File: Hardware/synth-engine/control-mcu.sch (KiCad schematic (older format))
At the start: 75 parts, among them J1 SWD_programming, J2 USB, J3 MIDI_IN, J4 MIDI_OUT, Q1 2N3904, U1 CY8C4246AZI-L445, U2 4N28, Y1 16MHz

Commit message: route 3.3VD voltage regulator and control MCU
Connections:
- net +5V: no longer C1.1, C3.1, C4.1, C5.1, C6.2, C7.1, C8.1, C9.2, J1.1 (Pin_1), R2.1, U1.11 (VDDA), U1.17 (VSSIO), U1.50 (VDDD), U1.56 (VDDA)
- net 3.3V: now also C1.1, C3.1, C4.1, C5.1, C6.2, C7.1, C8.1, C9.2, J1.1 (Pin_1), R2.1, U1.11 (VDDA), U1.17 (VSSIO), U1.50 (VDDD), U1.56 (VDDA)
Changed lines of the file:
@@
-	1    0    0    -1
-$EndComp
-$Comp
-L power:+5V #PWR012
-U 1 1 5DDBF5E4
-P 1400 1250
-F 0 "#PWR012" H 1400 1100 50  0001 C CNN
-F 1 "+5V" H 1415 1423 50  0000 C CNN
-F 2 "" H 1400 1250 50  0001 C CNN
-F 3 "" H 1400 1250 50  0001 C CNN
-	1    1400 1250
 	1    0    0    -1
 $EndComp
@@
 Wire Wire Line
 	1050 1800 1600 1800
-$Comp
-L power:+5V #PWR06
-U 1 1 5DDBF5FB
-P 950 2750
-F 0 "#PWR06" H 950 2600 50  0001 C CNN
-F 1 "+5V" H 965 2923 50  0000 C CNN
-F 2 "" H 950 2750 50  0001 C CNN
-F 3 "" H 950 2750 50  0001 C CNN
-	1    950  2750
-	1    0    0    -1
-$EndComp
 $Comp
 L power:GNDD #PWR07
@@
 Connection ~ 950  3000
 $Comp
-L power:+5V #PWR01
-U 1 1 5DDBF61B
-P 650 3200
-F 0 "#PWR01" H 650 3050 50  0001 C CNN
-F 1 "+5V" H 665 3373 50  0000 C CNN
-F 2 "" H 650 3200 50  0001 C CNN
-F 3 "" H 650 3200 50  0001 C CNN
-	1    650  3200
-	1    0    0    -1
-$EndComp
-$Comp
 L power:GNDD #PWR02
 U 1 1 5DDBF621
@@
 Connection ~ 650  3450
 $Comp
-L power:+5V #PWR04
-U 1 1 5DDBF63B
-P 850 3600
-F 0 "#PWR04" H 850 3450 50  0001 C CNN
-F 1 "+5V" H 950 3650 50  0000 C CNN
-F 2 "" H 850 3600 50  0001 C CNN
-F 3 "" H 850 3600 50  0001 C CNN
-	1    850  3600
-	1    0    0    -1
-$EndComp
-$Comp
 L power:GNDD #PWR05
 U 1 1 5DDBF641
@@
 Wire Wire Line
 	1600 3850 1600 3750
-$Comp
-L power:+5V #PWR09
-U 1 1 5DDBF65E
-P 1050 4250
-F 0 "#PWR09" H 1050 4100 50  0001 C CNN
-F 1 "+5V" H 1065 4423 50  0000 C CNN
-F 2 "" H 1050 4250 50  0001 C CNN
-F 3 "" H 1050 4250 50  0001 C CNN
-	1    1050 4250
-	1    0    0    1
-$EndComp
 $Comp
 L power:GNDD #PWR08
@@
 Wire Wire Line
 	1200 7250 950  7250
-$Comp
-L power:+5V #PWR010
-U 1 1 5DDBF6E8
-P 1050 7000
-F 0 "#PWR010" H 1050 6850 50  0001 C CNN
-F 1 "+5V" H 1150 7050 50  0000 C CNN
-F 2 "" H 1050 7000 50  0001 C CNN
-F 3 "" H 1050 7000 50  0001 C CNN
-	1    1050 7000
-	1    0    0    -1
-$EndComp
 Wire Wire Line
 	1050 7000 1050 7150
@@
 Wire Wire Line
 	1450 2350 1600 2350
+$Comp
+L SparkFun-Aesthetics:3.3V #SUPPLY?
+U 1 1 5DDD3D34
+P 1400 1250
+F 0 "#SUPPLY?" H 1400 1250 50  0001 L BNN
+F 1 "3.3V" H 1400 1424 50  0000 C CNN
+F 2 "" H 1400 1250 50  0001 C CNN
+F 3 "" H 1400 1250 50  0001 C CNN
+	1    1400 1250
+	1    0    0    -1
+$EndComp
+$Comp
+L SparkFun-Aesthetics:3.3V #SUPPLY?
+U 1 1 5DDD5545
+P 950 2750
+F 0 "#SUPPLY?" H 950 2750 50  0001 L BNN
+F 1 "3.3V" H 950 2924 50  0000 C CNN
+F 2 "" H 950 2750 50  0001 C CNN
+F 3 "" H 950 2750 50  0001 C CNN
+	1    950  2750
+	1    0    0    -1
+$EndComp
+$Comp
+L SparkFun-Aesthetics:3.3V #SUPPLY?
+U 1 1 5DDD6153
+P 650 3200
+F 0 "#SUPPLY?" H 650 3200 50  0001 L BNN
+F 1 "3.3V" H 650 3374 50  0000 C CNN
+F 2 "" H 650 3200 50  0001 C CNN
+F 3 "" H 650 3200 50  0001 C CNN
+	1    650  3200
+	1    0    0    -1
+$EndComp
+$Comp
+L SparkFun-Aesthetics:3.3V #SUPPLY?
+U 1 1 5DDD61F4
+P 850 3600
+F 0 "#SUPPLY?" H 850 3600 50  0001 L BNN
+F 1 "3.3V" H 1000 3650 50  0000 C CNN
+F 2 "" H 850 3600 50  0001 C CNN
+F 3 "" H 850 3600 50  0001 C CNN
+	1    850  3600
+	1    0    0    -1
+$EndComp
+$Comp
+L SparkFun-Aesthetics:3.3V #SUPPLY?
+U 1 1 5DDD6380
+P 1050 4250
+F 0 "#SUPPLY?" H 1050 4250 50  0001 L BNN
+F 1 "3.3V" H 1050 4424 50  0000 C CNN
+F 2 "" H 1050 4250 50  0001 C CNN
+F 3 "" H 1050 4250 50  0001 C CNN
+	1    1050 4250
+	-1   0    0    1
+$EndComp
+$Comp
+L SparkFun-Aesthetics:3.3V #SUPPLY?
+U 1 1 5DDD845B
+P 1050 7000
+F 0 "#SUPPLY?" H 1050 7000 50  0001 L BNN
+F 1 "3.3V" H 1050 7174 50  0000 C CNN
+F 2 "" H 1050 7000 50  0001 C CNN
+F 3 "" H 1050 7000 50  0001 C CNN
+	1    1050 7000
+	1    0    0    -1
+$EndComp
 $EndSCHEMATC

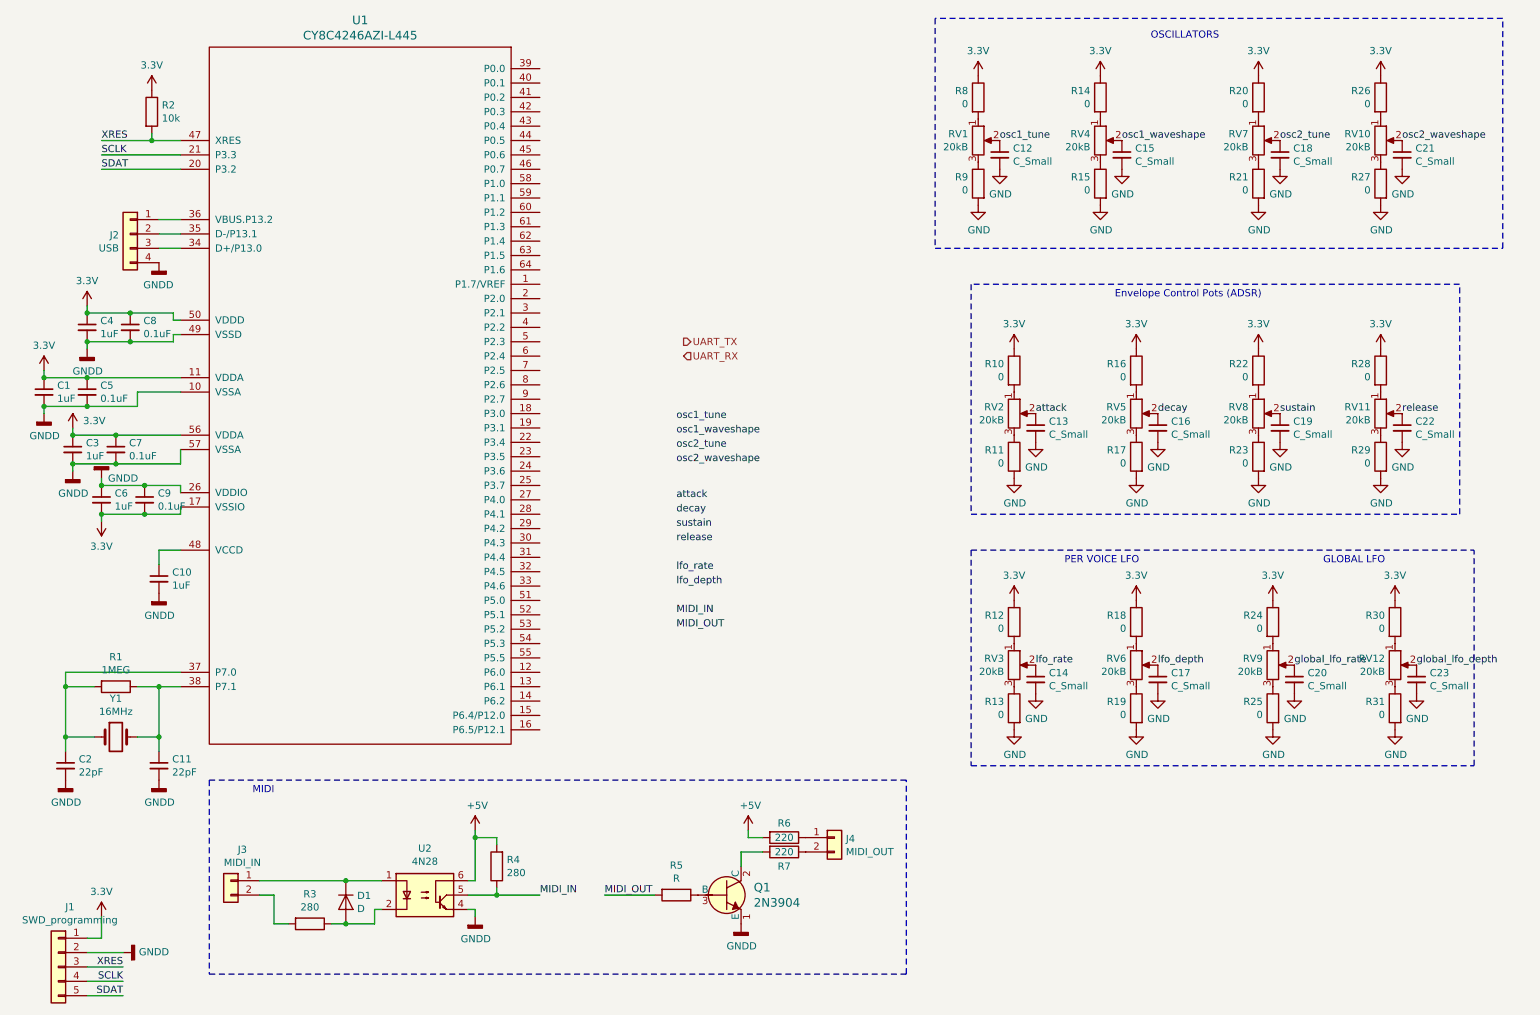
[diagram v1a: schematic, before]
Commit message: add separate PCB with potentiometers and switches and connector between control board and synth engine
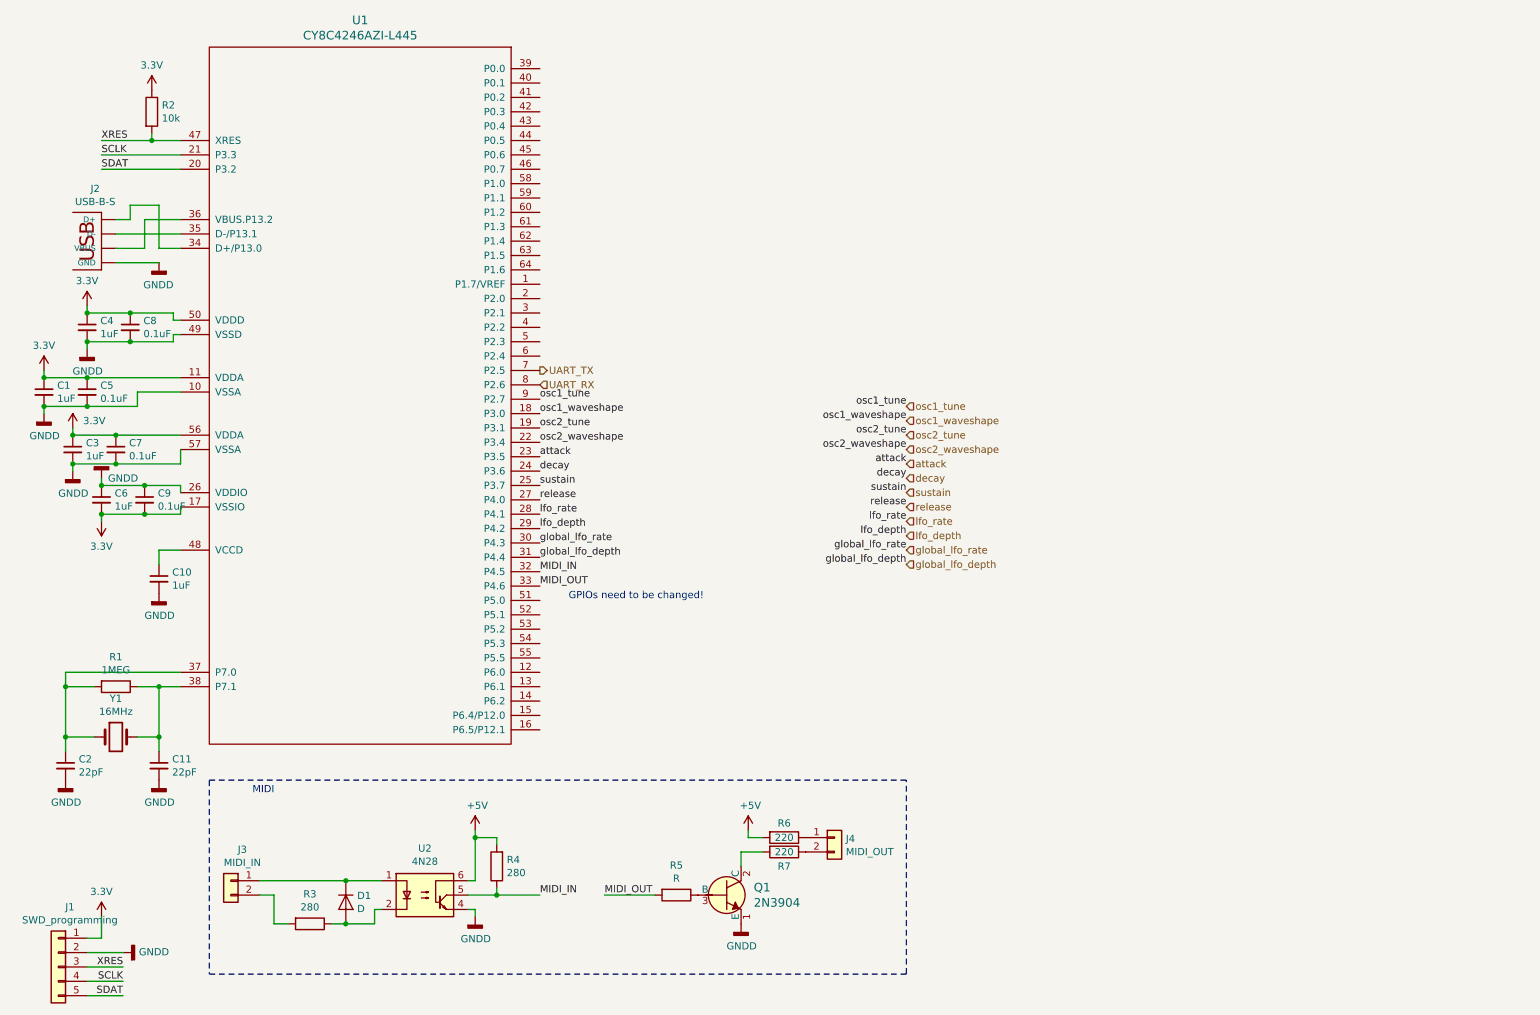
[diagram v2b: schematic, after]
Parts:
- removed C12, C13, C14, C15, C16, C17, C18, C19, C20, C21, C22, C23: C_Small, SparkFun-Passives:0805, symbol Device:C_Small
- removed J2: USB, SparkFun-Connectors:USB-B-PTH, symbol Connector_Generic:Conn_01x04
- removed R10, R11, R12, R13, R14, R15, R16, R17, R18, R19, R20, R21, R22, R23, R24, R25, R26, R27, R28, R29, R30, R31, R8, R9: 0, SparkFun-Passives:0805, symbol Device:R
- removed RV1, RV10, RV11, RV12, RV2, RV3, RV4, RV5, RV6, RV7, RV8, RV9: 20kB, Potentiometer_THT:Potentiometer_Alps_RK09K_Single_Vertical, symbol Device:R_POT
- added J2: USB-B-S, SparkFun-Connectors:USB-B-PTH, symbol SparkFun-Connectors:USB-B-S
- D1: footprint SparkFun-DiscreteSemi:SMB-DIODE -> SparkFun-Passives:1210
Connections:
- net GNDD: now also J2.GND
- net MIDI_IN: now also U1.32 (P4.5)
- net MIDI_OUT: now also U1.33 (P4.6)
- net UART_RX: now also U1.8 (P2.6)
- net UART_TX: now also U1.7 (P2.5)
- net attack: now also U1.23 (P3.5)
- net decay: now also U1.24 (P3.6)
- net global_lfo_depth: now also U1.31 (P4.4)
- net global_lfo_rate: now also U1.30 (P4.3)
- net lfo_depth: now also U1.29 (P4.2)
- net lfo_rate: now also U1.28 (P4.1)
- net osc1_tune: now also U1.9 (P2.7)
- net osc1_waveshape: now also U1.18 (P3.0)
- net osc2_tune: now also U1.19 (P3.1)
- net osc2_waveshape: now also U1.22 (P3.4)
- net release: now also U1.27 (P4.0)
- net sustain: now also U1.25 (P3.7)
- net at U1.34 (D+/P13.0): now also J2.D+
- net at U1.35 (D-/P13.1): now also J2.D-
- net at U1.36 (VBUS.P13.2): now also J2.VUSB (VBUS)
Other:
- note added: "GPIOs need to be changed!"
- note removed: "Envelope Control Pots (ADSR)"
- note removed: "GLOBAL LFO"
- note removed: "OSCILLATORS"
- note removed: "PER VOICE LFO"

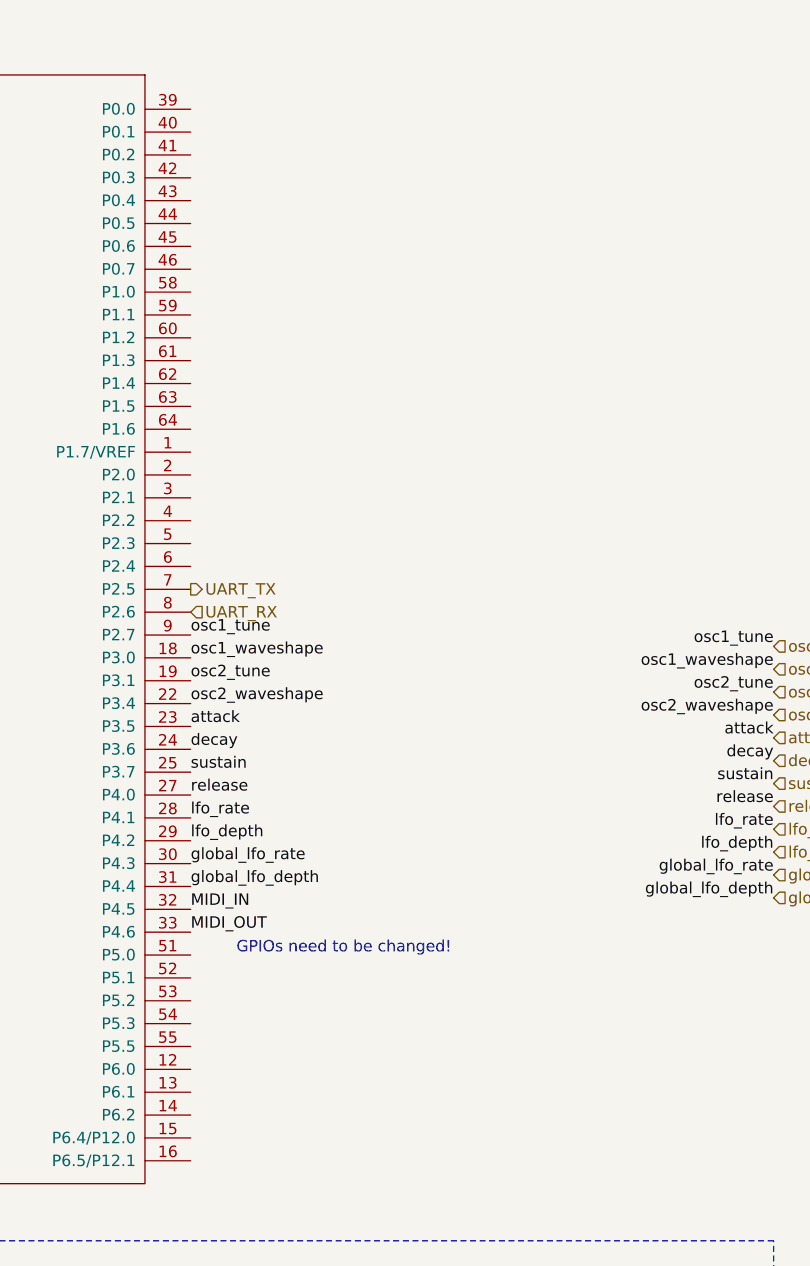
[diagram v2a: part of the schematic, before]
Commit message: initial routing complete. Still need to do ground plane pours. There are still some issues with incorrect footprints.
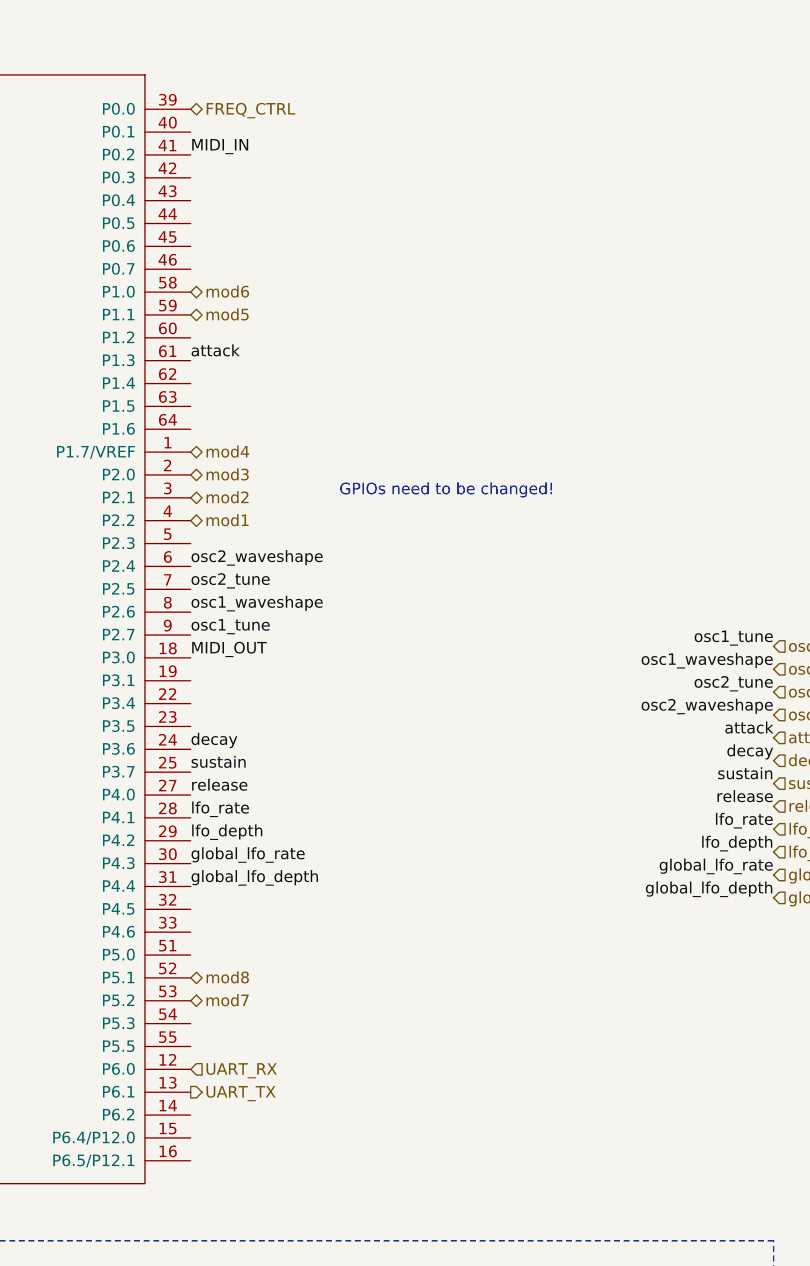
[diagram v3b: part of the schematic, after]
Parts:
- U2: footprint Package_DIP:DIP-6_W7.62mm -> SparkFun-AnalogIC:DIL-08
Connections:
- net MIDI_IN: now also U1.41 (P0.2); no longer U1.32 (P4.5)
- net MIDI_OUT: now also U1.18 (P3.0); no longer U1.33 (P4.6)
- net UART_RX: now also U1.12 (P6.0); no longer U1.8 (P2.6)
- net UART_TX: now also U1.13 (P6.1); no longer U1.7 (P2.5)
- net attack: now also U1.61 (P1.3); no longer U1.23 (P3.5)
- net osc1_waveshape: now also U1.8 (P2.6); no longer U1.18 (P3.0)
- net osc2_tune: now also U1.7 (P2.5); no longer U1.19 (P3.1)
- net osc2_waveshape: now also U1.6 (P2.4); no longer U1.22 (P3.4)
- net mod4: now reaches U1.1 (P1.7/VREF)
- net mod3: now reaches U1.2 (P2.0)
- net mod2: now reaches U1.3 (P2.1)
- net FREQ_CTRL: now reaches U1.39 (P0.0)
- net mod1: now reaches U1.4 (P2.2)
- net mod8: now reaches U1.52 (P5.1)
- net mod7: now reaches U1.53 (P5.2)
- net mod6: now reaches U1.58 (P1.0)
- net mod5: now reaches U1.59 (P1.1)
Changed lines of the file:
@@
 F 0 "U2" H 3300 7175 50  0000 C CNN
 F 1 "4N28" H 3300 7084 50  0000 C CNN
-F 2 "Package_DIP:DIP-6_W7.62mm" H 3100 6650 50  0001 L CIN
+F 2 "SparkFun-AnalogIC:DIL-08" H 3100 6650 50  0001 L CIN
 F 3 "https://www.vishay.com/docs/83725/4n25.pdf" H 3300 6850 50  0001 L CNN
 	1    3300 6850
@@
 Text Label 6650 4350 2    50   ~ 0
 lfo_depth
-Text Label 4100 4600 0    50   ~ 0
+Text Label 4100 1300 0    50   ~ 0
 MIDI_IN
-Text Label 4100 4700 0    50   ~ 0
+Text Label 4100 3500 0    50   ~ 0
 MIDI_OUT
 $Comp
@@
 Text Label 6650 3750 2    50   ~ 0
 osc2_waveshape
-Text HLabel 4100 3200 2    50   Output ~ 0
+Text HLabel 4100 5400 2    50   Output ~ 0
 UART_TX
-Text HLabel 4100 3300 2    50   Input ~ 0
+Text HLabel 4100 5300 2    50   Input ~ 0
 UART_RX
 Wire Wire Line
@@
 Text Label 6650 4550 2    50   ~ 0
 global_lfo_depth
-Text Label 4100 3800 0    50   ~ 0
+Text Label 4100 2200 0    50   ~ 0
 attack
 Text Label 4100 3900 0    50   ~ 0
@@
 Text Label 4100 3400 0    50   ~ 0
 osc1_tune
-Text Label 4100 3500 0    50   ~ 0
+Text Label 4100 3300 0    50   ~ 0
 osc1_waveshape
-Text Label 4100 3600 0    50   ~ 0
+Text Label 4100 3200 0    50   ~ 0
 osc2_tune
-Text Label 4100 3700 0    50   ~ 0
+Text Label 4100 3100 0    50   ~ 0
 osc2_waveshape
 Text Label 4100 4400 0    50   ~ 0
@@
 Text Label 4100 4500 0    50   ~ 0
 global_lfo_depth
-Text Notes 4300 4800 0    50   ~ 0
+Text Notes 4750 2800 0    50   ~ 0
 GPIOs need to be changed!
+Text HLabel 4100 1100 2    50   BiDi ~ 0
+FREQ_CTRL
+Text HLabel 4100 2900 2    50   BiDi ~ 0
+mod1
+Text HLabel 4100 2800 2    50   BiDi ~ 0
+mod2
+Text HLabel 4100 2700 2    50   BiDi ~ 0
+mod3
+Text HLabel 4100 2600 2    50   BiDi ~ 0
+mod4
+Text HLabel 4100 2000 2    50   BiDi ~ 0
+mod5
+Text HLabel 4100 1900 2    50   BiDi ~ 0
+mod6
+Text HLabel 4100 5000 2    50   BiDi ~ 0
+mod7
+Text HLabel 4100 4900 2    50   BiDi ~ 0
+mod8
 $EndSCHEMATC

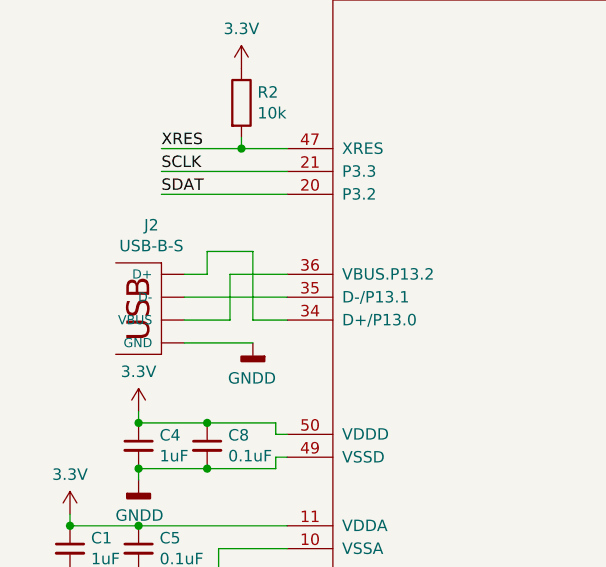
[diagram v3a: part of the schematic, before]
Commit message: fix some footprint errors
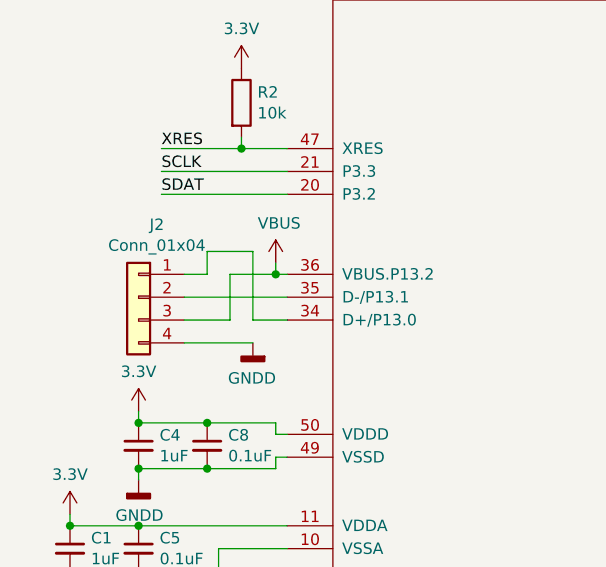
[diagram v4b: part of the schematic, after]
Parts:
- removed J2: USB-B-S, SparkFun-Connectors:USB-B-PTH, symbol SparkFun-Connectors:USB-B-S
- added J2: Conn_01x04, SparkFun-Connectors:1X04, symbol Connector_Generic:Conn_01x04
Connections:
- net GNDD: now also J2.4 (Pin_4)
- net at U1.34 (D+/P13.0): now also J2.1 (Pin_1)
- net at U1.35 (D-/P13.1): now also J2.2 (Pin_2)
- net VBUS: now reaches U1.36 (VBUS.P13.2)
- net VBUS: now also J2.3 (Pin_3)
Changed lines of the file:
@@
 	1    0    0    -1
-$EndComp
-$Comp
-L SparkFun-Connectors:USB-B-S J2
-U 1 1 5DDF016B
-P 1050 2450
-F 0 "J2" H 1094 2965 50  0000 C CNN
-F 1 "USB-B-S" H 1094 2874 50  0000 C CNN
-F 2 "SparkFun-Connectors:USB-B-PTH" H 1080 2600 20  0001 C CNN
-F 3 "" H 1050 2450 60  0000 C CNN
-	1    1050 2450
-	-1   0    0    -1
 $EndComp
 Wire Wire Line
@@
 	1350 2350 1350 2150
 Wire Wire Line
-	1350 2150 1600 2150
+	1350 2150 1550 2150
 Text HLabel 6650 3450 2    50   Input ~ 0
 osc1_tune
@@
 Text HLabel 4100 4900 2    50   BiDi ~ 0
 mod8
+$Comp
+L power:VBUS #PWR0121
+U 1 1 5DE5C7FD
+P 1550 2100
+F 0 "#PWR0121" H 1550 1950 50  0001 C CNN
+F 1 "VBUS" H 1565 2273 50  0000 C CNN
+F 2 "" H 1550 2100 50  0001 C CNN
+F 3 "" H 1550 2100 50  0001 C CNN
+	1    1550 2100
+	1    0    0    -1
+$EndComp
+Wire Wire Line
+	1550 2100 1550 2150
+Connection ~ 1550 2150
+Wire Wire Line
+	1550 2150 1600 2150
+$Comp
+L Connector_Generic:Conn_01x04 J2
+U 1 1 5DE792F8
+P 950 2250
+F 0 "J2" H 870 2567 50  0000 C CNN
+F 1 "Conn_01x04" H 870 2476 50  0000 C CNN
+F 2 "SparkFun-Connectors:1X04" H 950 2250 50  0001 C CNN
+F 3 "~" H 950 2250 50  0001 C CNN
+	1    950  2250
+	-1   0    0    -1
+$EndComp
 $EndSCHEMATC
